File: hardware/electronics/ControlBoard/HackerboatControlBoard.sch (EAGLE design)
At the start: 287 parts, among them IC1 74AHC1G08DBV, IC2 74AUC1G06DBV, IC3 74AHC1G04DBV, IC4 V7805, IC5 7805TV, T1 AO4407A, U1 IPS6041G, U10 INA169, U11 IPS6041G, U12 INA169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

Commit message: Control board BoM complete
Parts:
- 15V-ENB, H1, H3, H4, H7, J1, J10, J11, J2, J9, SJ1, U$1: PARTNO (none) -> ?
- 5V-STAT, 7V4-STAT, ENABLE, PWR, RLY0, RLY1, RLY2, RLY3, RLY4, RLY5: PARTNO * -> LG R971-KN-1
- BBB_CONSOLE: PARTNO * -> 215299-6
- BBB_RESET, RS485, STATUS_LIGHTS, STEERING: PARTNO * -> 0705550037
- BLOWN, FAULT_0, FAULT_1, FAULT_2, FAULT_3, FAULT_4, FAULT_5, FAULT_DISARM, FAULT_ENABLE, FAULT_HORN, HORN-RLY, REV: PARTNO * -> LH R974-LP-1
- C18, C20: PARTNO * -> GRM32ER61E226KE15K
- C26, C27, C43, C44: PARTNO * -> UMK325F475ZH
- C30: PARTNO * -> CL10B103KB8NCNC
- C31: PARTNO * -> CL10B822KB8SFNC
- C33: value 7u5 -> 7p5; PARTNO * -> CL10C7R5DB8NNNC
- C34: PARTNO * -> CL10B221KC8WPNC
- C41, C42, C49, C50: value 1000p -> 22n; PARTNO * -> CKCL44X5R1C223M085AA
- C45: PARTNO * -> C1608X7R1H473M
- C46: PARTNO * -> CL10C680JB8NNNC
- CELL: PARTNO * -> BCS-118-L-S-TE
- D1, D10, D11, D12, D14, D15, D16, D17, D18, D19, D2, D3, D4, D5, D6, D7, D8, D9: PARTNO * -> CDBW140-G
- D13: PARTNO * -> MMSZ4678-TP
- D20, D36: PARTNO * -> SK310A-LTP
- D21, D22, D23, D24, D25, D26, D27, D28: PARTNO * -> SMF5.0A
- DISARM: PARTNO * -> HSMA-C170
- ENABLE/DISARM, J3, J5, J6, J7, SJ2, U$2, U$3, U$4, U$5: BOM (none) -> EXCLUDE
- F2: PARTNO * -> MF-LSMF300/24X-2
- GPS: PARTNO * -> BCS-109-L-S-TE
- HORN: PARTNO * -> 0705550036
- IC1: PARTNO * -> MC74HC1G08DTT1G
- IC2: PARTNO * -> SN74LVC1G06DBVR
- IC3: PARTNO * -> MC74HC1G04DTT1G
- IC4: value V7805 -> V7805-2000; PARTNO (none) -> V7805-2000
- IC5: value 7805TV -> V7805-2000; PARTNO (none) -> V7805-2000
- IMU: PARTNO * -> BCS-110-L-S-TE
- L2: PARTNO * -> NR6045T220M
- L3: PARTNO * -> SRN8040-220M
- MOTOR-CTRL-RELAYS: PARTNO * -> 1734354-1
- POE-DEVICE, POE-LAN: PARTNO * -> 615008137121
- POWER_INPUT: PARTNO * -> NC6-P108-02
- POWER_STATE: PARTNO * -> 0705550039
- R10, R16, R31, R37, R4, R45, R72, R78, R84: PARTNO * -> CRCW0603100KFKEA
- R11, R17, R32, R40, R46, R5, R55, R73, R79, R85: PARTNO * -> PE2512FKE070R05L
- R110, R111, R112, R113: value (none) -> 10K; PARTNO * -> 742C083103JPTR
- R12, R18, R33, R41, R47, R56, R6, R74, R80, R86: PARTNO * -> ERJ-3EKF3302V
- R19, R20, R51, R52, R53, R54: PARTNO * -> RC1608J472CS
- R26: PARTNO * -> RC0603FR-0711K5L
- R27: PARTNO * -> RC0603FR-0710K2L
- R28: PARTNO * -> RC0603FR-071K24L
- R49: PARTNO * -> RC0603JR-07110KL
- R50: PARTNO * -> RC0603JR-0715KL
- R58: PARTNO * -> RC0603FR-07174KL
- R59: PARTNO * -> RC0603FR-071K62L
- R60: PARTNO * -> ERJ-3EKF1823V
- R61: PARTNO * -> RC0603FR-0716K2L
- SBUS-IN, SBUS-OUT: PARTNO * -> 0705450037
- SERIAL_CONSOLE: PARTNO * -> 0705550038
- U1, U11, U2, U20, U22, U24, U4, U6, U8: PARTNO * -> IPS6041GPBF
- U10, U12, U21, U23, U25, U27, U3, U5, U7, U9: PARTNO * -> INA169NA/3K
- U13, U16, U17: PARTNO * -> TXB0108PWR
- U15: PARTNO * -> TPS54331DR
- U18, U19: PARTNO * -> ADC128D818CIMTX
- U26: PARTNO * -> TXS0102DCURG4
- U28: PARTNO * -> SN75176BDR
- U29: PARTNO * -> TPS61175PWPR

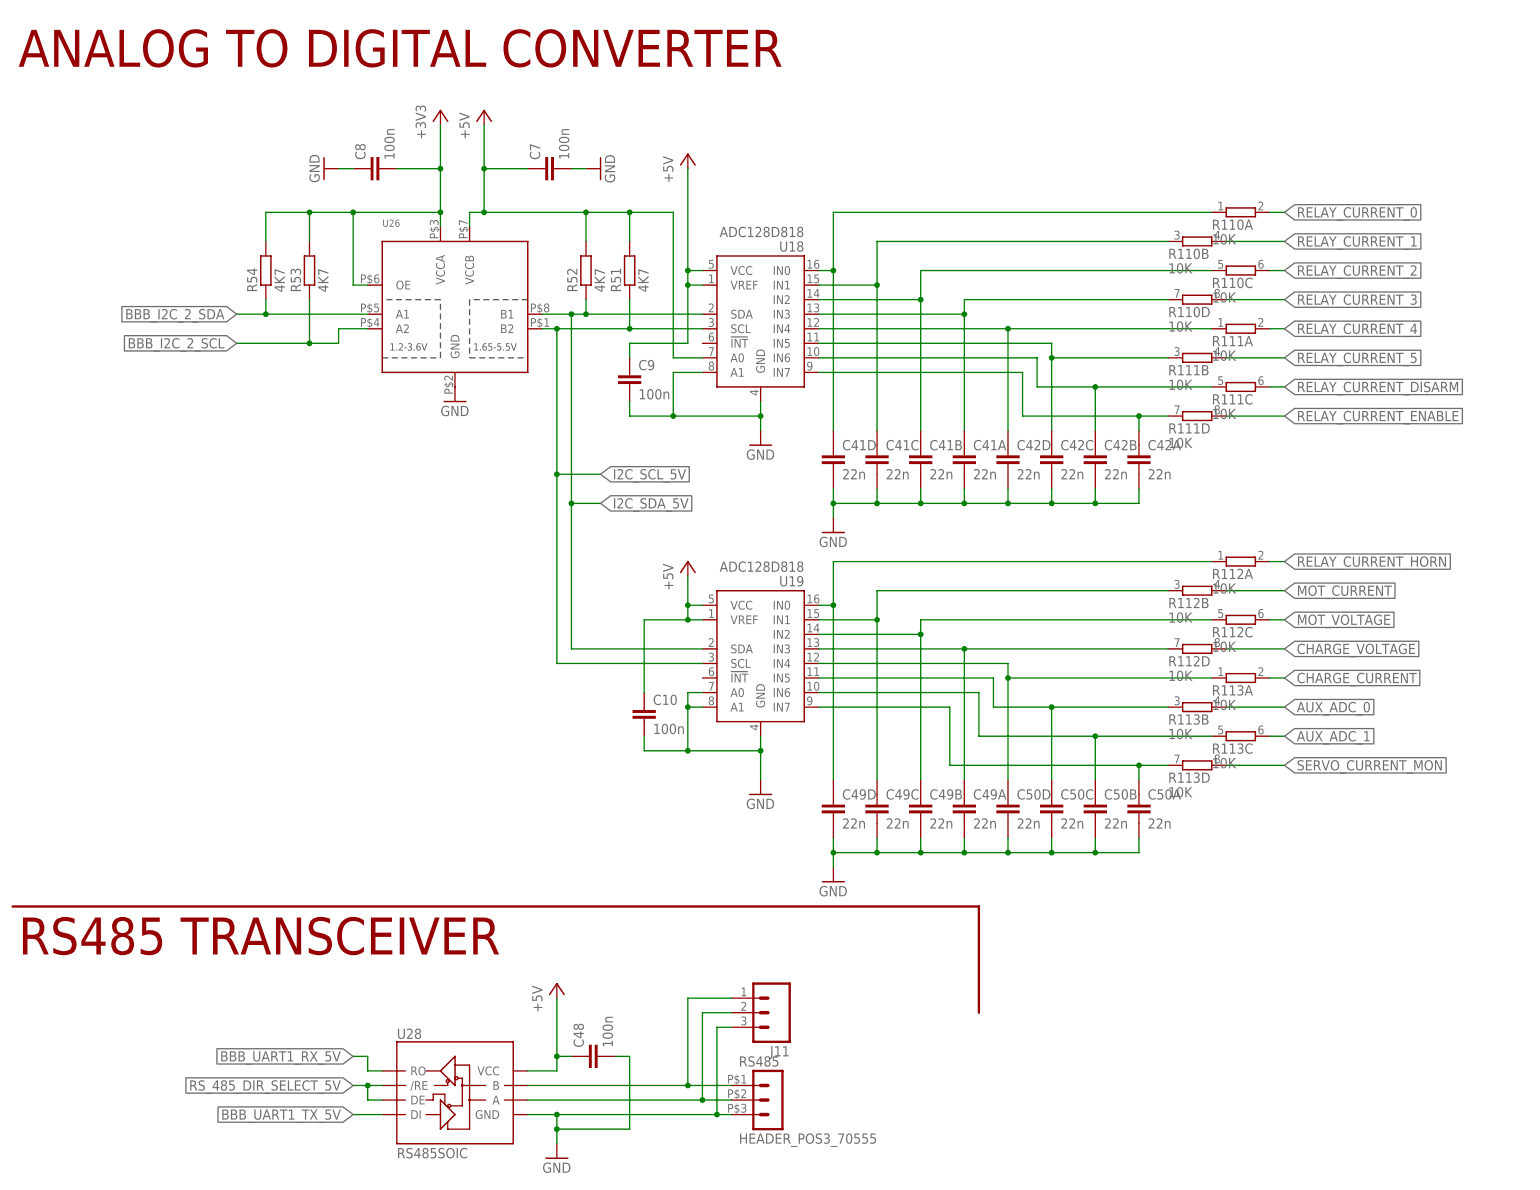
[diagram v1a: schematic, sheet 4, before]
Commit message: Added an Excel file documenting my pin mapping findings for the PWM subsystem. Made some minor changes to make the schematic more readable.
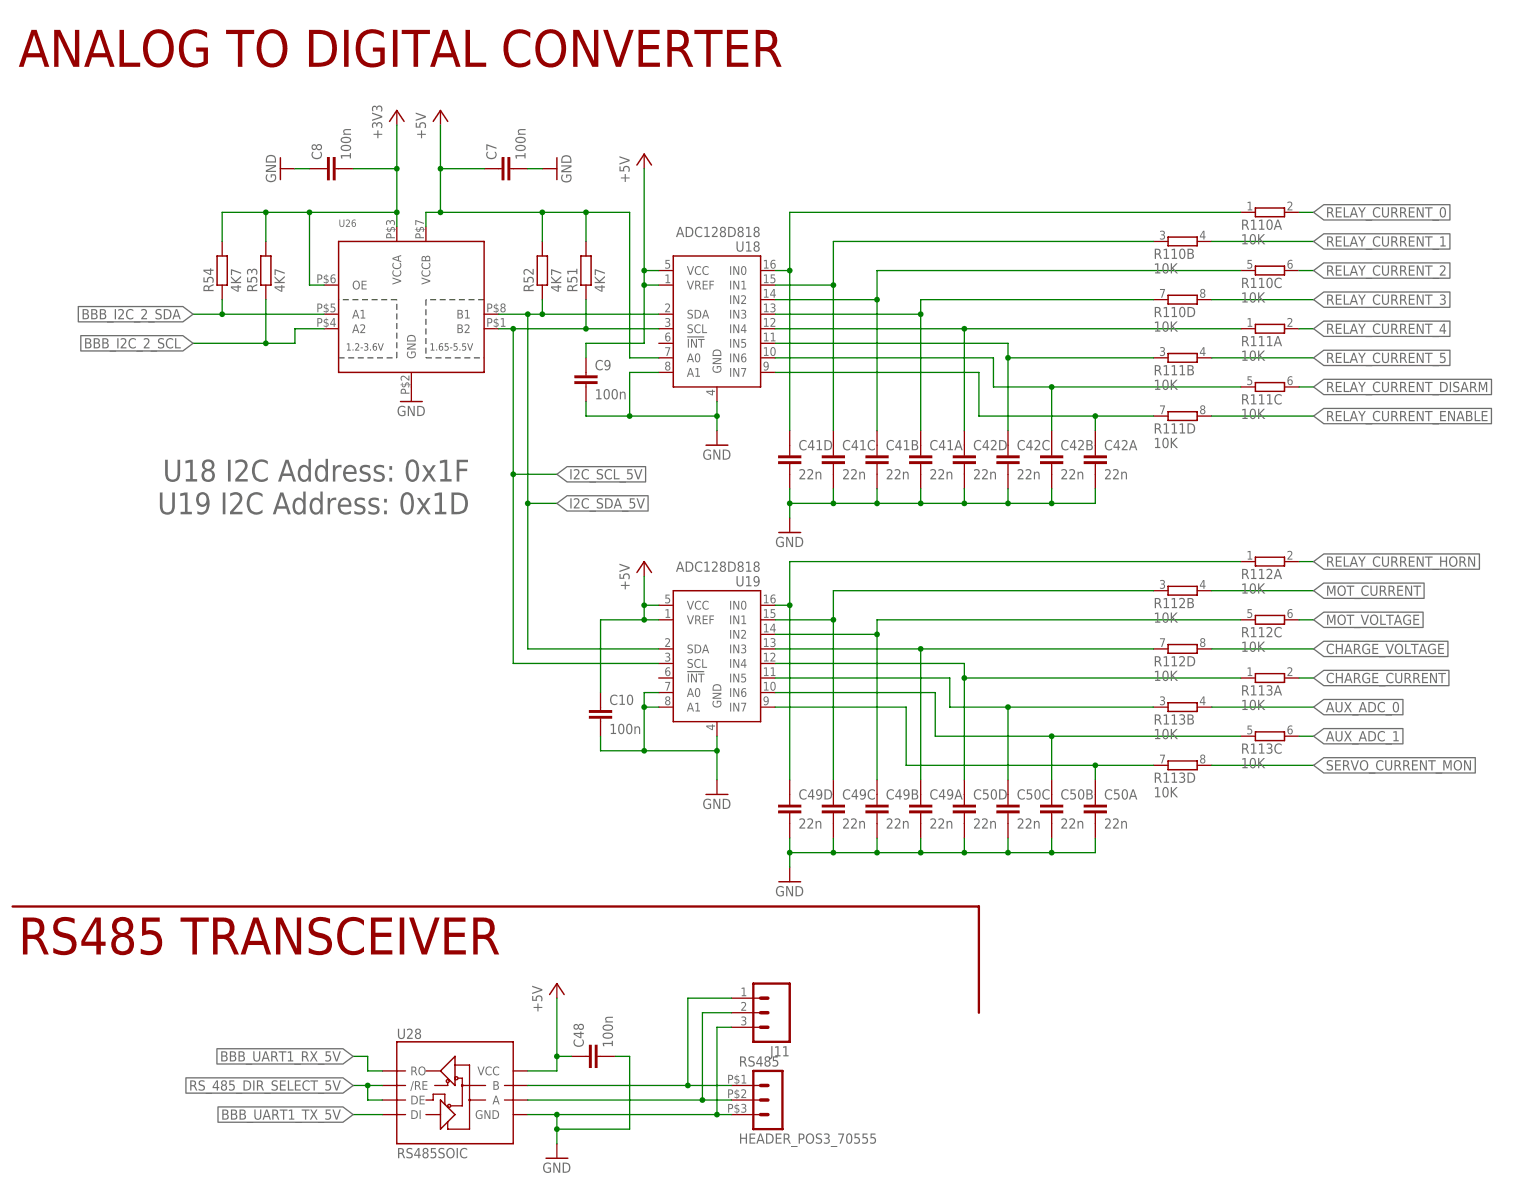
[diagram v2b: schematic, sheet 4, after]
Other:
- note added: "U18 I2C Address: 0x1F U19 I2C Address: 0x1D"
- moved on the sheet: C10, C41A, C41B, C41C, C41D, C42A, C42B, C42C, C42D, C49A, C49B, C49C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
